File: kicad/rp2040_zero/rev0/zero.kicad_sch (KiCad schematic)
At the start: 13 parts, among them J1 jtag, J2 Conn_01x03_Socket, J5 Debug port, U1 RP2040-Zero, U3 3V->VTREF, U4 VTREF->3V, U5 VTREF<->3V, U6 RT9013-33GB

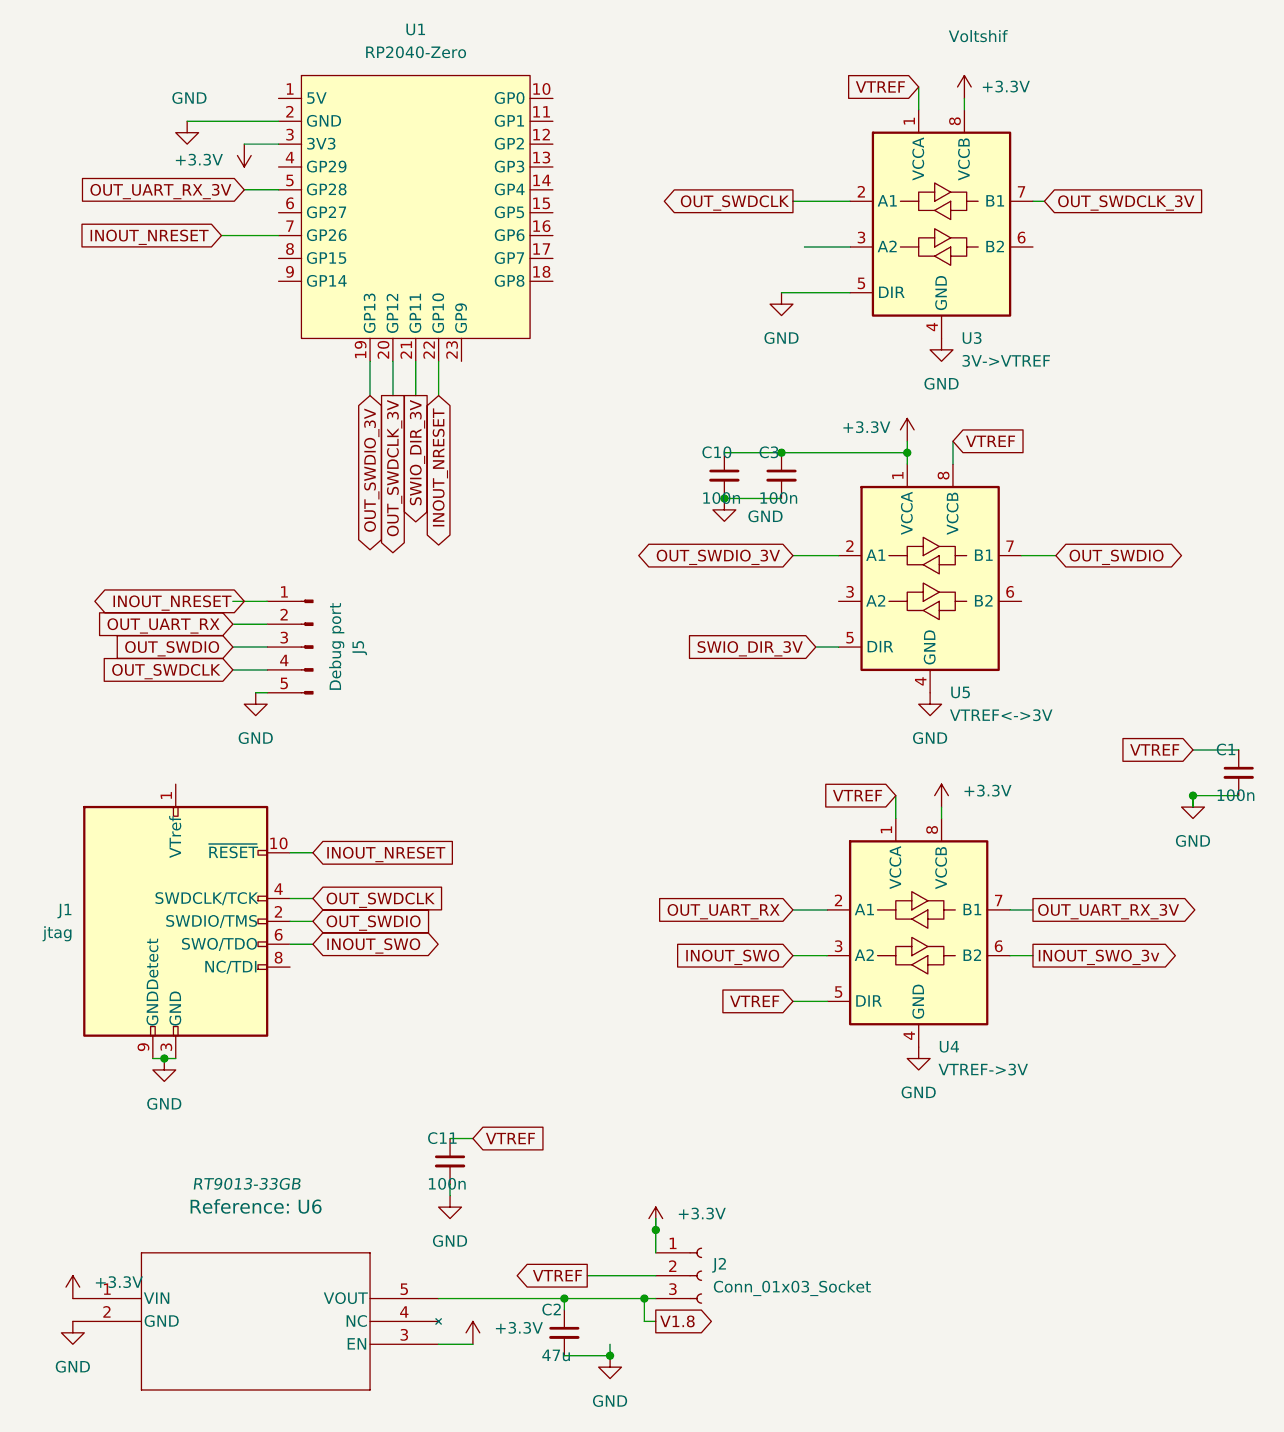
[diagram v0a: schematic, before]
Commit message: RP2040 : Add USE_RP2040 option to use the new PCB Kicad : RP2040 carrier layout mon : add mon enablereset to make exec from RAM work with vscode. That ignores the reset command sent by cortexdebug Misc : dont hardcode the target in the attach/vAttch command to 1.  Actually read the value.
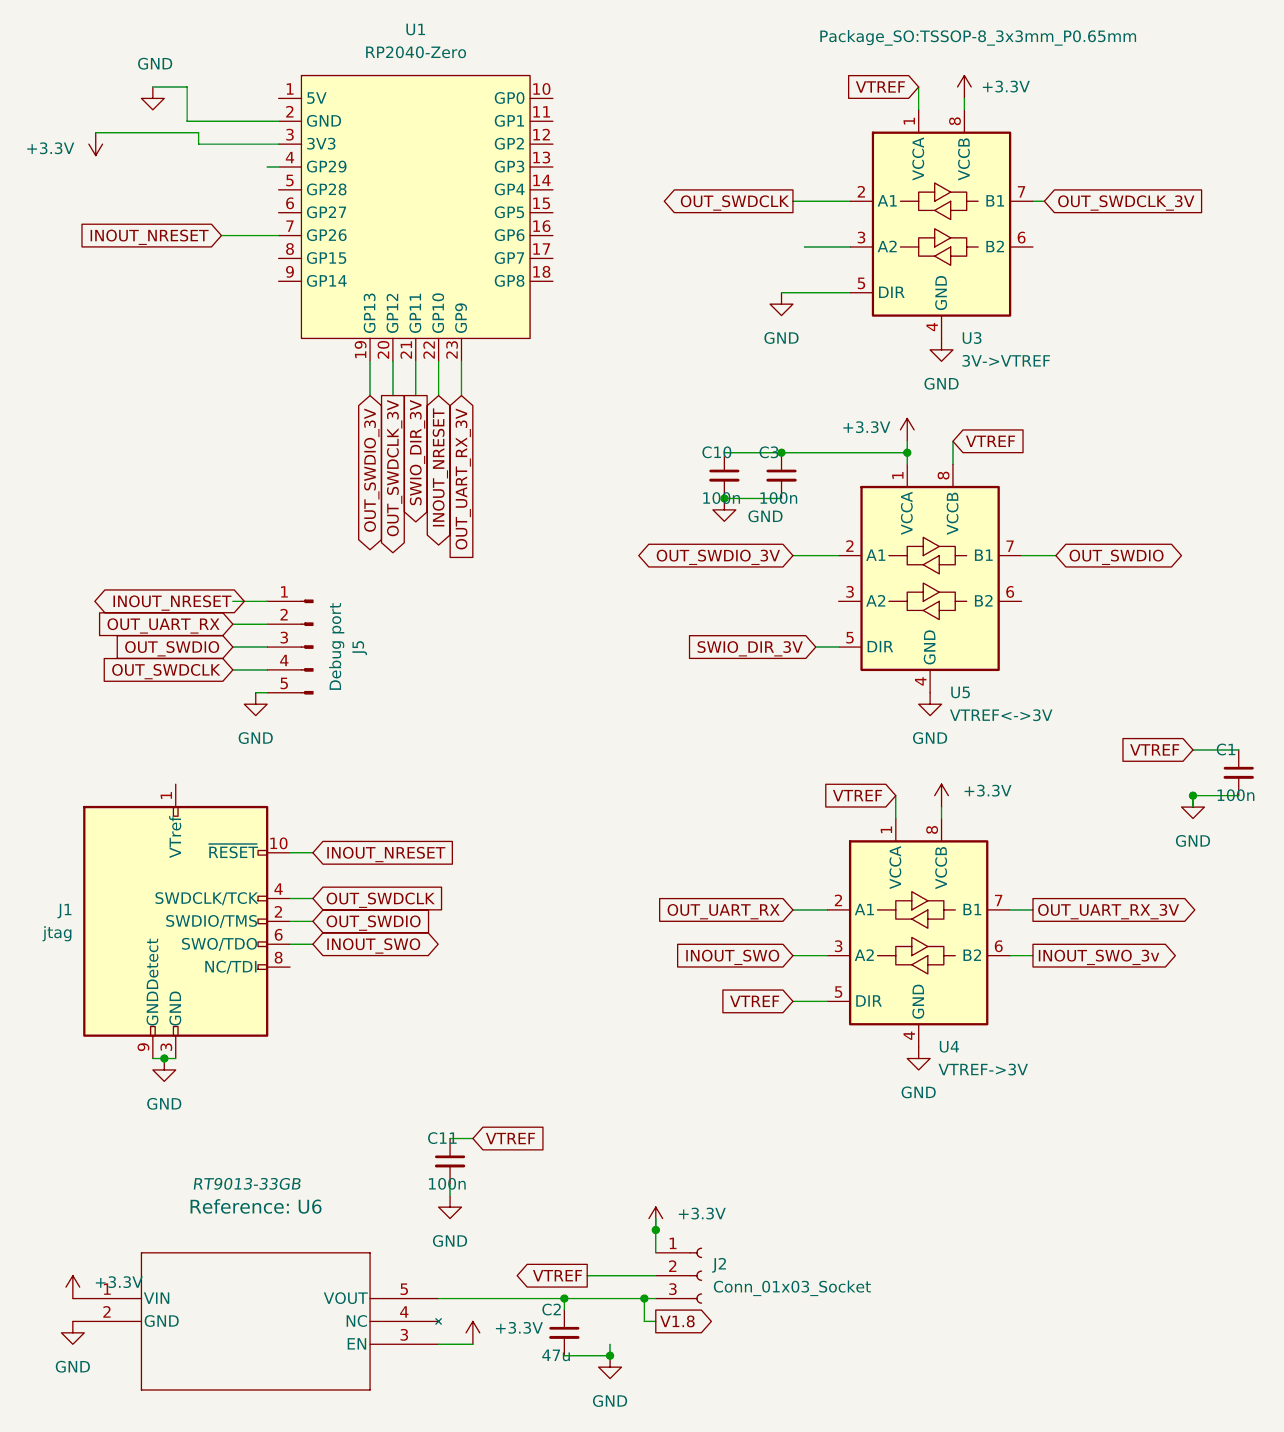
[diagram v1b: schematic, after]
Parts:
- U3: footprint Voltshif -> Package_SO:TSSOP-8_3x3mm_P0.65mm
- U4, U5: footprint Package_SO:VSSOP-8_2.3x2mm_P0.5mm -> Package_SO:TSSOP-8_3x3mm_P0.65mm
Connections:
- net OUT_UART_RX_3V: now also U1.23 (GP9); no longer U1.5 (GP28)
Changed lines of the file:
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@@
 	(wire
 		(pts
+			(xy 60.96 59.69) (xy 60.96 63.5)
+		)
+		(stroke
+			(width 0)
+			(type default)
+		)
+	)
+	(wire
+		(pts
+			(xy 31.75 35.56) (xy 40.64 35.56)
+		)
+		(stroke
+			(width 0)
+			(type default)
+		)
+	)
+	(wire
+		(pts
 			(xy 41.91 119.38) (xy 44.45 119.38)
 		)
@@
 	(wire
 		(pts
+			(xy 30.48 29.21) (xy 26.67 29.21)
+		)
+		(stroke
+			(width 0)
+			(type default)
+		)
+	)
+	(wire
+		(pts
 			(xy 123.19 81.28) (xy 127 81.28)
 		)
@@
 	(wire
 		(pts
-			(xy 36.83 35.56) (xy 40.64 35.56)
+			(xy 20.32 34.29) (xy 31.75 34.29)
 		)
 		(stroke
@@
 	(wire
 		(pts
+			(xy 39.37 38.1) (xy 40.64 38.1)
+		)
+		(stroke
+			(width 0)
+			(type default)
+		)
+	)
+	(wire
+		(pts
 			(xy 41.91 121.92) (xy 44.45 121.92)
 		)
@@
 	(wire
 		(pts
+			(xy 30.48 33.02) (xy 30.48 29.21)
+		)
+		(stroke
+			(width 0)
+			(type default)
+		)
+	)
+	(wire
+		(pts
 			(xy 82.55 156.21) (xy 82.55 158.75)
 		)
@@
 	(wire
 		(pts
-			(xy 142.24 102.87) (xy 147.32 102.87)
+			(xy 31.75 34.29) (xy 31.75 35.56)
 		)
 		(stroke
@@
 	(wire
 		(pts
-			(xy 58.42 163.83) (xy 72.39 163.83)
+			(xy 142.24 102.87) (xy 147.32 102.87)
 		)
 		(stroke
@@
 	(wire
 		(pts
-			(xy 100.33 91.44) (xy 102.87 91.44)
+			(xy 58.42 163.83) (xy 72.39 163.83)
 		)
 		(stroke
@@
 	(wire
 		(pts
-			(xy 115.57 68.58) (xy 115.57 71.12)
+			(xy 100.33 91.44) (xy 102.87 91.44)
 		)
 		(stroke
@@
 	(wire
 		(pts
-			(xy 58.42 59.69) (xy 58.42 63.5)
+			(xy 115.57 68.58) (xy 115.57 71.12)
 		)
 		(stroke
@@
 	(wire
 		(pts
-			(xy 36.83 40.64) (xy 40.64 40.64)
+			(xy 58.42 59.69) (xy 58.42 63.5)
 		)
 		(stroke
@@
 	(global_label "OUT_UART_RX_3V"
 		(shape input)
-		(at 36.83 40.64 180)
+		(at 60.96 63.5 270)
 		(fields_autoplaced yes)
 		(effects
@@
 		)
 		(property "Intersheetrefs" "${INTERSHEET_REFS}"
-			(at 17.8791 40.64 0)
+			(at 60.96 82.4509 90)
 			(effects
 				(font
@@
 			)
 		)
-		(property "Footprint" "Package_SO:VSSOP-8_2.3x2mm_P0.5mm"
+		(property "Footprint" "Package_SO:TSSOP-8_3x3mm_P0.65mm"
 			(at 114.3 97.79 0)
 			(effects
@@
 			)
 		)
-		(property "Footprint" "Voltshif"
+		(property "Footprint" "Package_SO:TSSOP-8_3x3mm_P0.65mm"
 			(at 118.364 23.622 0)
 			(effects
@@
 			)
 		)
-		(property "Footprint" "Package_SO:VSSOP-8_2.3x2mm_P0.5mm"
+		(property "Footprint" "Package_SO:TSSOP-8_3x3mm_P0.65mm"
 			(at 113.03 137.16 0)
 			(effects
@@
 	(symbol
 		(lib_id "power:+3.3V")
-		(at 36.83 35.56 180)
+		(at 20.32 34.29 180)
 		(unit 1)
 		(exclude_from_sim no)
@@
 		(dnp no)
 		(property "Reference" "#PWR01"
-			(at 36.83 31.75 0)
+			(at 20.32 30.48 0)
 			(effects
 				(font
@@
 		)
 		(property "Value" "+3.3V"
-			(at 31.75 37.338 0)
+			(at 15.24 36.068 0)
 			(effects
 				(font
@@
 		)
 		(property "Footprint" ""
-			(at 36.83 35.56 0)
+			(at 20.32 34.29 0)
 			(effects
 				(font
@@
 		)
 		(property "Datasheet" ""
-			(at 36.83 35.56 0)
+			(at 20.32 34.29 0)
 			(effects
 				(font
@@
 		)
 		(property "Description" ""
-			(at 36.83 35.56 0)
+			(at 20.32 34.29 0)
 			(effects
 				(font
@@
 	(symbol
 		(lib_id "power:GND")
-		(at 30.48 33.02 0)
+		(at 26.67 29.21 0)
 		(unit 1)
 		(exclude_from_sim no)
@@
 		(dnp no)
 		(property "Reference" "#PWR02"
-			(at 30.48 39.37 0)
+			(at 26.67 35.56 0)
 			(effects
 				(font
@@
 		)
 		(property "Value" "GND"
-			(at 30.734 30.48 0)
+			(at 26.924 26.67 0)
 			(effects
 				(font
@@
 		)
 		(property "Footprint" ""
-			(at 30.48 33.02 0)
+			(at 26.67 29.21 0)
 			(effects
 				(font
@@
 		)
 		(property "Datasheet" ""
-			(at 30.48 33.02 0)
+			(at 26.67 29.21 0)
 			(effects
 				(font
@@
 		)
 		(property "Description" ""
-			(at 30.48 33.02 0)
+			(at 26.67 29.21 0)
 			(effects
 				(font
